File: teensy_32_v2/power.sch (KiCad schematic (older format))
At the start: 31 parts, among them J1 277-1667-ND, J2 277-1667-ND, Q1 STL62P3LLH6, U2 MF-DSC-SOT233-BSS138, U3 DS7257G

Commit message: another attempt at Hat layout -- pre routing
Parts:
- removed D3: MF-DIO-SOD123-BAT42, MF_Discrete_Semiconductor:MF_Discrete_Semiconductor-SOD-123, symbol D_Schottky_Small
- added D3: MF-DIO-SOD123-BAT42, MF_Discrete_Semiconductor:MF_Discrete_Semiconductor-SOD-123, symbol DIODES_BAT42_SOD-123
- R1: value MF-RES-0805-6.8K -> MF-RES-0805-15K
- R16: value MF-RES-0805-10K -> MF-RES-0805-15K
- R2, R5: value MF-RES-0805-470 -> MF-RES-0604-2K; footprint MF_Passives:MF_Passives-R0805 -> MF_Passives:MF_Passives-R0603
- R4: value MF-RES-0805-220K -> MF-RES-0805-100K
- U3: footprint (none) -> teensy:DS7257G
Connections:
- net labels added: VIN, V_BOOT, V_COMP, V_EN, V_FB, V_SS, V_SW, V_VIN
- wire segments 119 -> 84
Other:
- moved on the sheet: C1, R5, R6, R7, R8

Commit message: Macrofab proto order of teensy hat v2b
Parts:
- D1: value PMEG3050EP,115 -> PMEG3050BEP,115
- R2, R5: value MF-RES-0604-2K -> MF-RES-0603-2K
- U3: value DS7257G -> RT7257G
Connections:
- net labels added: +12V
- net labels removed: +BATT
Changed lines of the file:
@@
 P 3500 3550
 F 0 "R2" V 3400 3400 45  0000 L BNN
-F 1 "MF-RES-0604-2K" V 3650 3150 45  0000 L BNN
+F 1 "MF-RES-0603-2K" V 3650 3150 45  0000 L BNN
 F 2 "MF_Passives:MF_Passives-R0603" H 3750 3460 20  0001 C CNN
 F 3 "" H 3500 3550 60  0001 C CNN
@@
 P 4350 3650
 F 0 "R5" V 4300 3800 45  0000 L BNN
-F 1 "MF-RES-0604-2K" V 4500 3250 45  0000 L BNN
+F 1 "MF-RES-0603-2K" V 4500 3250 45  0000 L BNN
 F 2 "MF_Passives:MF_Passives-R0603" H 4600 3560 20  0001 C CNN
 F 3 "" H 4350 3650 60  0001 C CNN
@@
 Text HLabel 4350 3200 1    60   Input ~ 0
 PWR_ON
-$Comp
-L +BATT #PWR013
-U 1 1 59F4C39F
-P 4800 1800
-F 0 "#PWR013" H 4800 1650 50  0001 C CNN
-F 1 "+BATT" H 4800 1940 50  0000 C CNN
-F 2 "" H 4800 1800 50  0001 C CNN
-F 3 "" H 4800 1800 50  0001 C CNN
-	1    4800 1800
-	1    0    0    -1
-$EndComp
 $Comp
 L RESISTOR_0805 R6
@@
 $EndComp
 $Comp
-L GND #PWR014
+L GND #PWR013
 U 1 1 59F4C528
 P 4800 5400
-F 0 "#PWR014" H 4800 5150 50  0001 C CNN
+F 0 "#PWR013" H 4800 5150 50  0001 C CNN
 F 1 "GND" H 4800 5250 50  0000 C CNN
 F 2 "" H 4800 5400 50  0001 C CNN
@@
 $EndComp
 $Comp
-L GND #PWR015
+L GND #PWR014
 U 1 1 59F4D21D
 P 10100 3100
-F 0 "#PWR015" H 10100 2850 50  0001 C CNN
+F 0 "#PWR014" H 10100 2850 50  0001 C CNN
 F 1 "GND" H 10100 2950 50  0000 C CNN
 F 2 "" H 10100 3100 50  0001 C CNN
@@
 P 6550 2750
 F 0 "D1" H 6550 2850 50  0000 C CNN
-F 1 "PMEG3050EP,115" H 6500 2650 50  0000 C CNN
+F 1 "PMEG3050BEP,115" H 6500 2650 50  0000 C CNN
 F 2 "teensy:SOD-128" H 6550 2750 50  0001 C CNN
 F 3 "" H 6550 2750 50  0001 C CNN
@@
 $EndComp
 $Comp
-L GND #PWR016
+L GND #PWR015
 U 1 1 59F6D5D8
 P 5450 5400
-F 0 "#PWR016" H 5450 5150 50  0001 C CNN
+F 0 "#PWR015" H 5450 5150 50  0001 C CNN
 F 1 "GND" H 5450 5250 50  0000 C CNN
 F 2 "" H 5450 5400 50  0001 C CNN
@@
 $EndComp
 $Comp
-L GND #PWR017
+L GND #PWR016
 U 1 1 59F6EFD6
 P 10300 6000
-F 0 "#PWR017" H 10300 5750 50  0001 C CNN
+F 0 "#PWR016" H 10300 5750 50  0001 C CNN
 F 1 "GND" H 10300 5850 50  0000 C CNN
 F 2 "" H 10300 6000 50  0001 C CNN
@@
 $EndComp
 $Comp
-L +5V #PWR018
+L +5V #PWR017
 U 1 1 59F6FD39
 P 10650 3400
-F 0 "#PWR018" H 10650 3250 50  0001 C CNN
+F 0 "#PWR017" H 10650 3250 50  0001 C CNN
 F 1 "+5V" H 10650 3540 50  0000 C CNN
 F 2 "" H 10650 3400 50  0001 C CNN
@@
 Connection ~ 4800 2050
 $Comp
-L PWR_FLAG #FLG019
+L PWR_FLAG #FLG018
 U 1 1 59F88A4B
 P 4400 1900
-F 0 "#FLG019" H 4400 1975 50  0001 C CNN
+F 0 "#FLG018" H 4400 1975 50  0001 C CNN
 F 1 "PWR_FLAG" H 4400 2050 50  0000 C CNN
 F 2 "" H 4400 1900 50  0001 C CNN
@@
 P 8200 4150
 F 0 "U3" H 7850 4850 60  0000 C CNN
-F 1 "DS7257G" H 8350 4850 60  0000 C CNN
+F 1 "RT7257G" H 8350 4850 60  0000 C CNN
 F 2 "teensy:DS7257G" H 8200 4150 60  0001 C CNN
 F 3 "" H 8200 4150 60  0001 C CNN
@@
 Text Label 1900 2400 0    60   ~ 0
 VIN
-Text Label 8200 2400 0    60   ~ 0
-+BATT
 Wire Wire Line
 	1450 4300 1100 4300
@@
 Connection ~ 1450 4300
 $Comp
-L PWR_FLAG #FLG020
+L PWR_FLAG #FLG019
 U 1 1 5A1AA244
 P 1100 4200
-F 0 "#FLG020" H 1100 4275 50  0001 C CNN
+F 0 "#FLG019" H 1100 4275 50  0001 C CNN
 F 1 "PWR_FLAG" H 1100 4350 50  0000 C CNN
 F 2 "" H 1100 4200 50  0001 C CNN
@@
 	1    0    0    -1
 $EndComp
+$Comp
+L +12V #PWR020
+U 1 1 5A1C26B3
+P 4800 1800
+F 0 "#PWR020" H 4800 1650 50  0001 C CNN
+F 1 "+12V" H 4800 1940 50  0000 C CNN
+F 2 "" H 4800 1800 50  0001 C CNN
+F 3 "" H 4800 1800 50  0001 C CNN
+	1    4800 1800
+	1    0    0    -1
+$EndComp
+Text Label 7850 2400 0    60   ~ 0
++12V
 $EndSCHEMATC

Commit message: update teensy hat schematic
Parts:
- added D5: MF-LED-0603-GREEN, MF_LEDs:MF_LEDs-LED0603, symbol LED_SINGLE-0603-GREEN
- added R11: MF-RES-0603-2K, MF_Passives:MF_Passives-R0603, symbol RESISTOR_0805
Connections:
- net +5V: now also R11.2
- net GND: now also D5.CATH (CATHODE)
- new net: D5.ANOD (ANODE), R11.1
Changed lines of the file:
@@
 $EndComp
 $Comp
-L GND #PWR010
+L GND #PWR011
 U 1 1 59F4B4F0
 P 1450 4350
-F 0 "#PWR010" H 1450 4100 50  0001 C CNN
+F 0 "#PWR011" H 1450 4100 50  0001 C CNN
 F 1 "GND" H 1450 4200 50  0000 C CNN
 F 2 "" H 1450 4350 50  0001 C CNN
@@
 $EndComp
 $Comp
-L GND #PWR011
+L GND #PWR012
 U 1 1 59F4B9A6
 P 3500 5400
-F 0 "#PWR011" H 3500 5150 50  0001 C CNN
+F 0 "#PWR012" H 3500 5150 50  0001 C CNN
 F 1 "GND" H 3500 5250 50  0000 C CNN
 F 2 "" H 3500 5400 50  0001 C CNN
@@
 $EndComp
 $Comp
-L +5V #PWR012
+L +5V #PWR013
 U 1 1 59F4C0D1
 P 4000 3350
-F 0 "#PWR012" H 4000 3200 50  0001 C CNN
+F 0 "#PWR013" H 4000 3200 50  0001 C CNN
 F 1 "+5V" H 4000 3490 50  0000 C CNN
 F 2 "" H 4000 3350 50  0001 C CNN
@@
 $EndComp
 $Comp
-L GND #PWR013
+L GND #PWR014
 U 1 1 59F4C528
 P 4800 5400
-F 0 "#PWR013" H 4800 5150 50  0001 C CNN
+F 0 "#PWR014" H 4800 5150 50  0001 C CNN
 F 1 "GND" H 4800 5250 50  0000 C CNN
 F 2 "" H 4800 5400 50  0001 C CNN
@@
 $EndComp
 $Comp
-L GND #PWR014
+L GND #PWR015
 U 1 1 59F4D21D
 P 10100 3100
-F 0 "#PWR014" H 10100 2850 50  0001 C CNN
+F 0 "#PWR015" H 10100 2850 50  0001 C CNN
 F 1 "GND" H 10100 2950 50  0000 C CNN
 F 2 "" H 10100 3100 50  0001 C CNN
@@
 $EndComp
 $Comp
-L GND #PWR015
+L GND #PWR016
 U 1 1 59F6D5D8
 P 5450 5400
-F 0 "#PWR015" H 5450 5150 50  0001 C CNN
+F 0 "#PWR016" H 5450 5150 50  0001 C CNN
 F 1 "GND" H 5450 5250 50  0000 C CNN
 F 2 "" H 5450 5400 50  0001 C CNN
@@
 $EndComp
 $Comp
-L GND #PWR016
+L GND #PWR017
 U 1 1 59F6EFD6
 P 10300 6000
-F 0 "#PWR016" H 10300 5750 50  0001 C CNN
+F 0 "#PWR017" H 10300 5750 50  0001 C CNN
 F 1 "GND" H 10300 5850 50  0000 C CNN
 F 2 "" H 10300 6000 50  0001 C CNN
@@
 $EndComp
 $Comp
-L +5V #PWR017
+L +5V #PWR018
 U 1 1 59F6FD39
 P 10650 3400
-F 0 "#PWR017" H 10650 3250 50  0001 C CNN
+F 0 "#PWR018" H 10650 3250 50  0001 C CNN
 F 1 "+5V" H 10650 3540 50  0000 C CNN
 F 2 "" H 10650 3400 50  0001 C CNN
@@
 Connection ~ 4800 2050
 $Comp
-L PWR_FLAG #FLG018
+L PWR_FLAG #FLG019
 U 1 1 59F88A4B
 P 4400 1900
-F 0 "#FLG018" H 4400 1975 50  0001 C CNN
+F 0 "#FLG019" H 4400 1975 50  0001 C CNN
 F 1 "PWR_FLAG" H 4400 2050 50  0000 C CNN
 F 2 "" H 4400 1900 50  0001 C CNN
@@
 Connection ~ 1450 4300
 $Comp
-L PWR_FLAG #FLG019
+L PWR_FLAG #FLG020
 U 1 1 5A1AA244
 P 1100 4200
-F 0 "#FLG019" H 1100 4275 50  0001 C CNN
+F 0 "#FLG020" H 1100 4275 50  0001 C CNN
 F 1 "PWR_FLAG" H 1100 4350 50  0000 C CNN
 F 2 "" H 1100 4200 50  0001 C CNN
@@
 $EndComp
 $Comp
-L +12V #PWR020
+L +12V #PWR021
 U 1 1 5A1C26B3
 P 4800 1800
-F 0 "#PWR020" H 4800 1650 50  0001 C CNN
+F 0 "#PWR021" H 4800 1650 50  0001 C CNN
 F 1 "+12V" H 4800 1940 50  0000 C CNN
 F 2 "" H 4800 1800 50  0001 C CNN
@@
 Text Label 7850 2400 0    60   ~ 0
 +12V
+$Comp
+L +5V #PWR022
+U 1 1 5A46F868
+P 2000 5250
+F 0 "#PWR022" H 2000 5100 50  0001 C CNN
+F 1 "+5V" H 2000 5390 50  0000 C CNN
+F 2 "" H 2000 5250 50  0001 C CNN
+F 3 "" H 2000 5250 50  0001 C CNN
+	1    2000 5250
+	1    0    0    -1
+$EndComp
+$Comp
+L RESISTOR_0805 R11
+U 1 1 5A46FB81
+P 2000 5550
+F 0 "R11" V 1900 5500 45  0000 L BNN
+F 1 "MF-RES-0603-2K" V 2150 5150 45  0000 L BNN
+F 2 "MF_Passives:MF_Passives-R0603" H 2250 5460 20  0001 C CNN
+F 3 "" H 2000 5550 60  0001 C CNN
+	1    2000 5550
+	1    0    0    1
+$EndComp
+$Comp
+L LED_SINGLE-0603-GREEN D5
+U 1 1 5A4701C7
+P 2000 6000
+F 0 "D5" H 1950 5850 45  0000 L BNN
+F 1 "MF-LED-0603-GREEN" H 1600 5750 45  0000 L BNN
+F 2 "MF_LEDs:MF_LEDs-LED0603" H 2040 5770 20  0001 C CNN
+F 3 "" H 2000 6000 60  0001 C CNN
+	1    2000 6000
+	0    1    1    0
+$EndComp
+$Comp
+L GND #PWR023
+U 1 1 5A47026F
+P 2000 6200
+F 0 "#PWR023" H 2000 5950 50  0001 C CNN
+F 1 "GND" H 2000 6050 50  0000 C CNN
+F 2 "" H 2000 6200 50  0001 C CNN
+F 3 "" H 2000 6200 50  0001 C CNN
+	1    2000 6200
+	1    0    0    -1
+$EndComp
+Wire Wire Line
+	2000 5250 2000 5350
+Wire Wire Line
+	2000 5750 2000 5900
+Wire Wire Line
+	2000 6100 2000 6200
 $EndSCHEMATC

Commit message: version 2017-12-30 of hat
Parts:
- added D7: ESD9M5.0ST5G, teensy:SOD-923, symbol D_Zener
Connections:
- net +5V: now also D7.1 (K)
- net GND: now also D7.2 (A)
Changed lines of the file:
@@
 P 2000 6000
 F 0 "D5" H 1950 5850 45  0000 L BNN
-F 1 "MF-LED-0603-GREEN" H 1600 5750 45  0000 L BNN
+F 1 "MF-LED-0603-GREEN" H 1600 6300 45  0000 L BNN
 F 2 "MF_LEDs:MF_LEDs-LED0603" H 2040 5770 20  0001 C CNN
 F 3 "" H 2000 6000 60  0001 C CNN
@@
 Wire Wire Line
 	2000 6100 2000 6200
+$Comp
+L +5V #PWR024
+U 1 1 5A485BDB
+P 1200 5250
+F 0 "#PWR024" H 1200 5100 50  0001 C CNN
+F 1 "+5V" H 1200 5390 50  0000 C CNN
+F 2 "" H 1200 5250 50  0001 C CNN
+F 3 "" H 1200 5250 50  0001 C CNN
+	1    1200 5250
+	1    0    0    -1
+$EndComp
+$Comp
+L GND #PWR025
+U 1 1 5A485C49
+P 1200 6250
+F 0 "#PWR025" H 1200 6000 50  0001 C CNN
+F 1 "GND" H 1200 6100 50  0000 C CNN
+F 2 "" H 1200 6250 50  0001 C CNN
+F 3 "" H 1200 6250 50  0001 C CNN
+	1    1200 6250
+	1    0    0    -1
+$EndComp
+$Comp
+L D_Zener D7
+U 1 1 5A485C98
+P 1200 5750
+F 0 "D7" H 1200 5900 50  0000 C CNN
+F 1 "ESD9M5.0ST5G" H 1200 5650 50  0000 C CNN
+F 2 "teensy:SOD-923" H 1200 5750 50  0001 C CNN
+F 3 "" H 1200 5750 50  0001 C CNN
+	1    1200 5750
+	0    1    1    0
+$EndComp
+Wire Wire Line
+	1200 5600 1200 5250
+Wire Wire Line
+	1200 5900 1200 6250
 $EndSCHEMATC

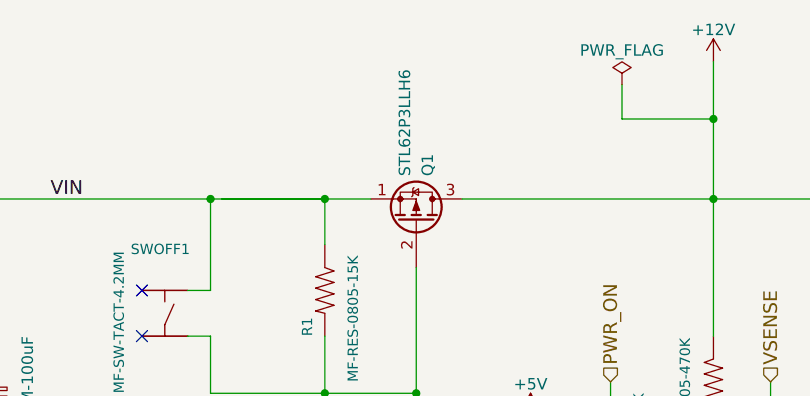
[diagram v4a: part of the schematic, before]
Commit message: update footprint for MOSFET
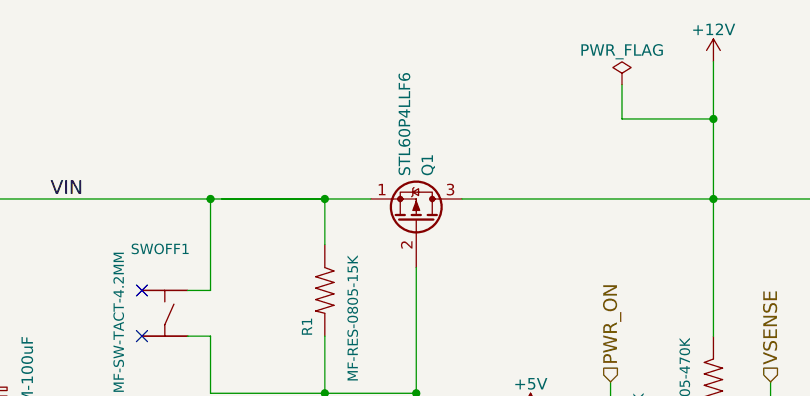
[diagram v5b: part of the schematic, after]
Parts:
- Q1: value STL62P3LLH6 -> STL60P4LLF6
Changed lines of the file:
@@
 P 3500 2500
 F 0 "Q1" H 3700 2550 50  0000 L CNN
-F 1 "STL62P3LLH6" H 3700 2450 50  0000 L CNN
+F 1 "STL60P4LLF6" H 3700 2450 50  0000 L CNN
 F 2 "teensy:POWERFLAT_5x6" H 3700 2600 50  0001 C CNN
 F 3 "" H 3500 2500 50  0001 C CNN

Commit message: tvs/zener protections
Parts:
- added D8: SMAJ16A-E3/61, Diodes_SMD:D_SMA_Standard, symbol D_Zener
- added D9: 824500850, Diodes_SMD:D_SMA_Standard, symbol D_Zener
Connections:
- net GND: now also D8.2 (A)
- net VIN: now also D9.1 (K)
- net V_VIN: now also D8.1 (K)
- net at Q1.2 (G), R1.2, R2.1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: now also D9.2 (A)
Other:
- note added: "10V"
- moved on the sheet: C6, C8, R1, R16, SWOFF1, SWON1
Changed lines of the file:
@@
 L GND #PWR011
 U 1 1 59F4B4F0
-P 1450 4350
-F 0 "#PWR011" H 1450 4100 50  0001 C CNN
-F 1 "GND" H 1450 4200 50  0000 C CNN
-F 2 "" H 1450 4350 50  0001 C CNN
-F 3 "" H 1450 4350 50  0001 C CNN
-	1    1450 4350
+P 1350 4350
+F 0 "#PWR011" H 1350 4100 50  0001 C CNN
+F 1 "GND" H 1350 4200 50  0000 C CNN
+F 2 "" H 1350 4350 50  0001 C CNN
+F 3 "" H 1350 4350 50  0001 C CNN
+	1    1350 4350
 	1    0    0    -1
 $EndComp
@@
 L RESISTOR_0805 R1
 U 1 1 59F4B601
-P 3100 2800
-F 0 "R1" V 3050 2600 45  0000 L BNN
-F 1 "MF-RES-0805-15K" V 3250 2400 45  0000 L BNN
-F 2 "MF_Passives:MF_Passives-R0805" H 3350 2710 20  0001 C CNN
-F 3 "" H 3100 2800 60  0001 C CNN
-	1    3100 2800
+P 3150 2800
+F 0 "R1" V 3100 2600 45  0000 L BNN
+F 1 "MF-RES-0805-15K" V 3300 2400 45  0000 L BNN
+F 2 "MF_Passives:MF_Passives-R0805" H 3400 2710 20  0001 C CNN
+F 3 "" H 3150 2800 60  0001 C CNN
+	1    3150 2800
 	1    0    0    -1
 $EndComp
@@
 L TACT_4.2MM SWOFF1
 U 1 1 59F4C815
-P 2400 2900
-F 0 "SWOFF1" H 2290 3180 45  0000 L CNN
-F 1 "MF-SW-TACT-4.2MM" V 2600 2550 45  0000 L CNN
-F 2 "MF_Switches:MF_Switches-TACT4.2MM" H 2290 3050 20  0001 L CNN
-F 3 "" H 2400 2900 60  0001 C CNN
-	1    2400 2900
+P 2400 2800
+F 0 "SWOFF1" H 2300 3000 45  0000 L CNN
+F 1 "MF-SW-TACT-4.2MM" V 2600 2450 45  0000 L CNN
+F 2 "MF_Switches:MF_Switches-TACT4.2MM" H 2290 2950 20  0001 L CNN
+F 3 "" H 2400 2800 60  0001 C CNN
+	1    2400 2800
 	-1   0    0    -1
 $EndComp
@@
 L TACT_4.2MM SWON1
 U 1 1 59F4D2A5
-P 2900 4400
-F 0 "SWON1" H 2790 4680 45  0000 L CNN
-F 1 "MF-SW-TACT-4.2MM" H 2790 4610 45  0000 L CNN
-F 2 "MF_Switches:MF_Switches-TACT4.2MM" H 2790 4550 20  0001 L CNN
-F 3 "" H 2900 4400 60  0001 C CNN
-	1    2900 4400
+P 2850 4750
+F 0 "SWON1" H 2740 5030 45  0000 L CNN
+F 1 "MF-SW-TACT-4.2MM" H 2740 4960 45  0000 L CNN
+F 2 "MF_Switches:MF_Switches-TACT4.2MM" H 2740 4900 20  0001 L CNN
+F 3 "" H 2850 4750 60  0001 C CNN
+	1    2850 4750
 	-1   0    0    -1
 $EndComp
@@
 L CAPACITOR_NP_0805 C6
 U 1 1 59F6A956
-P 6000 4850
-F 0 "C6" V 5950 4650 45  0000 L BNN
-F 1 "MF-CAP-0603-4.7nF" V 6150 4450 45  0000 L BNN
-F 2 "MF_Passives:MF_Passives-C0603" H 6250 4760 20  0001 C CNN
-F 3 "" H 6000 4850 60  0001 C CNN
-	1    6000 4850
+P 6500 4850
+F 0 "C6" V 6450 4650 45  0000 L BNN
+F 1 "MF-CAP-0603-4.7nF" V 6650 4450 45  0000 L BNN
+F 2 "MF_Passives:MF_Passives-C0603" H 6750 4760 20  0001 C CNN
+F 3 "" H 6500 4850 60  0001 C CNN
+	1    6500 4850
 	1    0    0    -1
 $EndComp
@@
 	1200 2400 3300 2400
 Wire Wire Line
-	2650 2400 3100 2400
-Wire Wire Line
 	3700 2400 10300 2400
 Wire Wire Line
-	1200 2500 1450 2500
-Wire Wire Line
-	1450 2500 1450 4350
-Wire Wire Line
-	3100 2400 3100 2600
-Wire Wire Line
-	3100 3000 3100 3250
+	1200 2500 1350 2500
+Wire Wire Line
+	1350 2500 1350 4350
+Wire Wire Line
+	3150 2400 3150 2600
+Wire Wire Line
+	3150 3250 3150 3000
 Wire Wire Line
 	2600 3250 3500 3250
@@
 	3500 3900 3100 3900
 Wire Wire Line
-	3100 3900 3100 4300
-Wire Wire Line
-	3100 4300 3000 4300
+	3100 3900 3100 4650
+Wire Wire Line
+	3100 4650 2950 4650
 Connection ~ 3500 3900
 Wire Wire Line
-	3100 5150 3100 4500
-Wire Wire Line
-	3100 4500 3000 4500
-Wire Wire Line
-	2500 2800 2600 2800
-Wire Wire Line
-	2600 2800 2600 2400
-Wire Wire Line
-	2600 3250 2600 3000
-Wire Wire Line
-	2600 3000 2500 3000
-Connection ~ 3100 3250
+	3100 5150 3100 4850
+Wire Wire Line
+	3100 4850 2950 4850
+Wire Wire Line
+	2500 2700 2600 2700
+Wire Wire Line
+	2600 2700 2600 2400
+Wire Wire Line
+	2600 3250 2600 2900
+Wire Wire Line
+	2600 2900 2500 2900
+Connection ~ 3150 3250
 Wire Wire Line
 	10300 2500 10100 2500
@@
 Wire Wire Line
 	4350 4350 4350 3850
-Connection ~ 3100 2400
+Connection ~ 3150 2400
 Connection ~ 2600 2400
 Connection ~ 6550 3750
@@
 	8850 3850 9000 3850
 Wire Wire Line
-	6000 4150 6000 4750
-Wire Wire Line
-	6000 5300 6000 4950
+	6500 4150 6500 4750
+Wire Wire Line
+	6500 5300 6500 4950
 Connection ~ 5450 5300
 Wire Wire Line
 	7100 5300 7100 4950
-Connection ~ 6000 5300
+Connection ~ 6500 5300
 Connection ~ 7100 5300
 Wire Wire Line
@@
 	1    0    0    -1
 $EndComp
-NoConn ~ 2300 2800
-NoConn ~ 2300 3000
-NoConn ~ 2800 4300
-NoConn ~ 2800 4500
+NoConn ~ 2300 2700
+NoConn ~ 2300 2900
+NoConn ~ 2750 4650
+NoConn ~ 2750 4850
 $Comp
 L DS7257G U3
@@
 	6050 3750 7550 3750
 Wire Wire Line
-	6550 3950 6700 3950
+	6150 3950 6700 3950
 Wire Wire Line
 	7100 3950 7550 3950
@@
 L RESISTOR_0805 R16
 U 1 1 59FE5CBE
-P 6550 4150
-F 0 "R16" V 6500 4250 45  0000 L BNN
-F 1 "MF-RES-0805-15K" V 6700 3800 45  0000 L BNN
-F 2 "MF_Passives:MF_Passives-R0805" H 6800 4060 20  0001 C CNN
-F 3 "" H 6550 4150 60  0001 C CNN
-	1    6550 4150
+P 6900 4150
+F 0 "R16" V 6850 4250 45  0000 L BNN
+F 1 "MF-RES-0805-15K" V 7050 3800 45  0000 L BNN
+F 2 "MF_Passives:MF_Passives-R0805" H 7150 4060 20  0001 C CNN
+F 3 "" H 6900 4150 60  0001 C CNN
+	1    6900 4150
 	0    -1   1    0
 $EndComp
 Wire Wire Line
-	6350 4150 6000 4150
-Wire Wire Line
-	6750 4150 7550 4150
+	6700 4150 6500 4150
+Wire Wire Line
+	7100 4150 7550 4150
 Wire Wire Line
 	10100 3600 10650 3600
@@
 L CP_Small C8
 U 1 1 59FE7D60
-P 1650 3250
-F 0 "C8" V 1600 3050 50  0000 L CNN
-F 1 "MF-CAP-6.3MM-100uF" V 1800 2750 50  0000 L CNN
-F 2 "MF_Passives:MF_Passives-CP6.3MM" H 1650 3250 50  0001 C CNN
-F 3 "" H 1650 3250 50  0001 C CNN
-	1    1650 3250
-	1    0    0    -1
-$EndComp
-Wire Wire Line
-	1650 3150 1650 2400
-Connection ~ 1650 2400
-Wire Wire Line
-	1650 3350 1650 3850
-Wire Wire Line
-	1650 3850 1450 3850
-Connection ~ 1450 3850
+P 1550 3350
+F 0 "C8" V 1500 3150 50  0000 L CNN
+F 1 "MF-CAP-6.3MM-100uF" V 1700 2850 50  0000 L CNN
+F 2 "MF_Passives:MF_Passives-CP6.3MM" H 1550 3350 50  0001 C CNN
+F 3 "" H 1550 3350 50  0001 C CNN
+	1    1550 3350
+	1    0    0    -1
+$EndComp
+Wire Wire Line
+	1550 3250 1550 2400
+Connection ~ 1550 2400
+Wire Wire Line
+	1550 4300 1550 3450
+Wire Wire Line
+	1100 4300 1550 4300
+Connection ~ 1350 4300
 $Comp
 L DIODES_BAT42_SOD-123 D3
@@
 Text Label 9000 3600 0    60   ~ 0
 V_BOOT
-Text Label 1900 2400 0    60   ~ 0
+Text Label 1250 2400 0    60   ~ 0
 VIN
 Wire Wire Line
-	1450 4300 1100 4300
-Wire Wire Line
 	1100 4300 1100 4200
-Connection ~ 1450 4300
 $Comp
 L PWR_FLAG #FLG020
@@
 Wire Wire Line
 	1200 5900 1200 6250
+$Comp
+L D_Zener D8
+U 1 1 5A4B06E7
+P 6150 4550
+F 0 "D8" H 6200 4450 50  0000 C CNN
+F 1 "SMAJ16A-E3/61" H 6150 4650 50  0000 C CNN
+F 2 "Diodes_SMD:D_SMA_Standard" H 6150 4550 50  0001 C CNN
+F 3 "" H 6150 4550 50  0001 C CNN
+	1    6150 4550
+	0    1    1    0
+$EndComp
+$Comp
+L D_Zener D9
+U 1 1 5A4B3289
+P 2850 2800
+F 0 "D9" H 2900 2700 50  0000 C CNN
+F 1 "824500850" H 2850 2900 50  0000 C CNN
+F 2 "Diodes_SMD:D_SMA_Standard" H 2850 2800 50  0001 C CNN
+F 3 "" H 2850 2800 50  0001 C CNN
+	1    2850 2800
+	0    1    1    0
+$EndComp
+Wire Wire Line
+	2850 2650 2850 2400
+Connection ~ 2850 2400
+Wire Wire Line
+	2850 2950 2850 3250
+Connection ~ 2850 3250
+Text Notes 2800 2750 1    47   ~ 0
+10V
+Wire Wire Line
+	6150 3950 6150 4400
+Connection ~ 6550 3950
+Wire Wire Line
+	6150 4700 6150 5300
+Connection ~ 6150 5300
 $EndSCHEMATC

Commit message: more work on teensy shield
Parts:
- D7, D8, D9: symbol D_Zener -> D_Zener-RESCUE-teensy_32_v2
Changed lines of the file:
@@
 EESchema Schematic File Version 2
+LIBS:teensy_32_v2-rescue
 LIBS:power
 LIBS:device
@@
 $EndComp
 $Comp
-L D_Zener D7
+L D_Zener-RESCUE-teensy_32_v2 D7
 U 1 1 5A485C98
 P 1200 5750
+AR Path="/5A485C98" Ref="D7"  Part="1"
+AR Path="/59ED6513/5A485C98" Ref="D7"  Part="1"
 F 0 "D7" H 1200 5900 50  0000 C CNN
 F 1 "ESD9M5.0ST5G" H 1200 5650 50  0000 C CNN
@@
 	1200 5900 1200 6250
 $Comp
-L D_Zener D8
+L D_Zener-RESCUE-teensy_32_v2 D8
 U 1 1 5A4B06E7
 P 6150 4550
+AR Path="/5A4B06E7" Ref="D8"  Part="1"
+AR Path="/59ED6513/5A4B06E7" Ref="D8"  Part="1"
 F 0 "D8" H 6200 4450 50  0000 C CNN
 F 1 "SMAJ16A-E3/61" H 6150 4650 50  0000 C CNN
@@
 $EndComp
 $Comp
-L D_Zener D9
+L D_Zener-RESCUE-teensy_32_v2 D9
 U 1 1 5A4B3289
 P 2850 2800
+AR Path="/5A4B3289" Ref="D9"  Part="1"
+AR Path="/59ED6513/5A4B3289" Ref="D9"  Part="1"
 F 0 "D9" H 2900 2700 50  0000 C CNN
 F 1 "824500850" H 2850 2900 50  0000 C CNN

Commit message: teensy hat updates
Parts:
- added D10: SMCJ15A, Diodes_SMD:D_SMC_Standard, symbol D_Zener
- added J10: 0878980426, Pin_Headers:Pin_Header_Straight_1x04_Pitch2.54mm_SMD_Pin1Right, symbol Conn_01x04
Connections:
- net GND: now also D10.2 (A), J10.1 (Pin_1)
- net VIN: now also D10.1 (K), J10.4 (Pin_4)
- net at D9.2, Q1.2 (G), R1.2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: now also J10.3 (Pin_3)
- net at R2.2, SWON1.1, U2.3 (DRAIN): now also J10.2 (Pin_2)
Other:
- moved on the sheet: C2, C3, C4, D5, D7, R11
